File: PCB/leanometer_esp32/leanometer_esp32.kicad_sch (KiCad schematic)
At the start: 5 parts

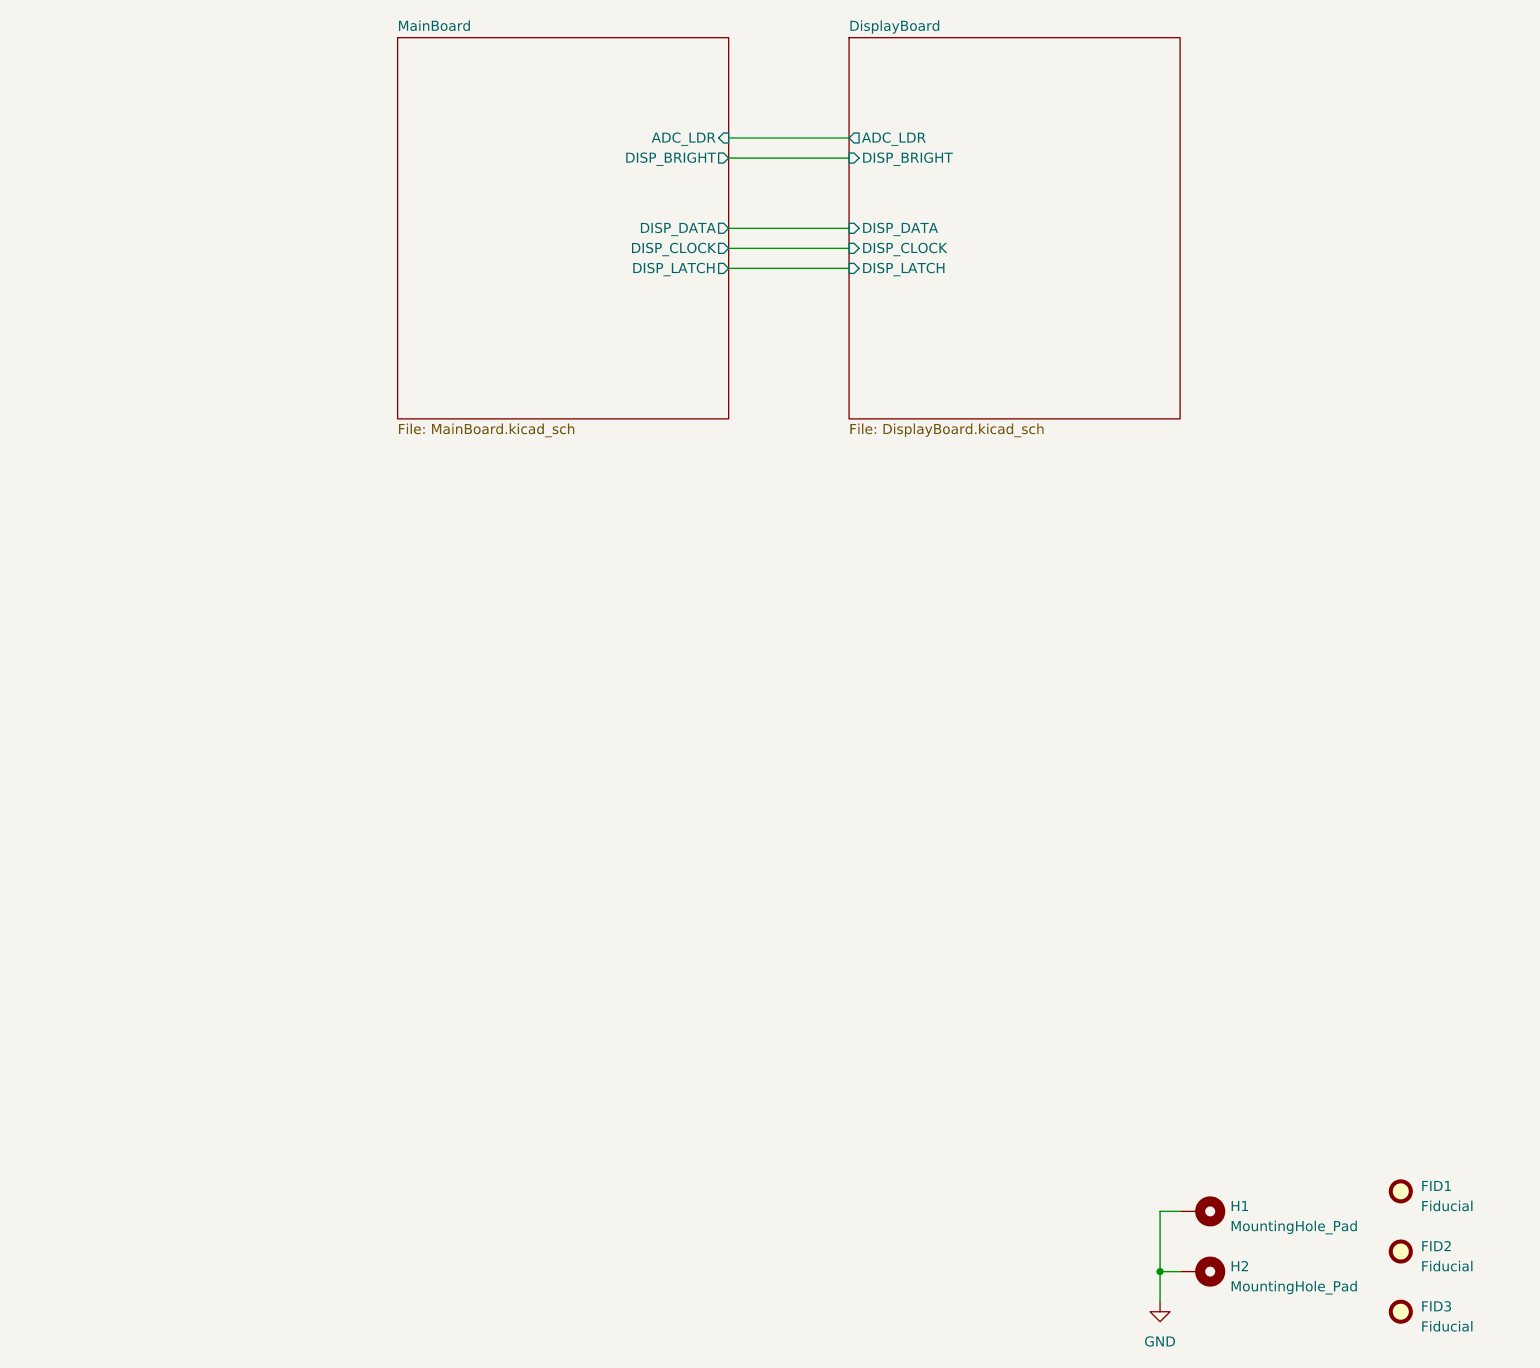
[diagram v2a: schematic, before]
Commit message: Added PowerBoard hierarchical sheet, completed layout
Signed-off-by: theloukou
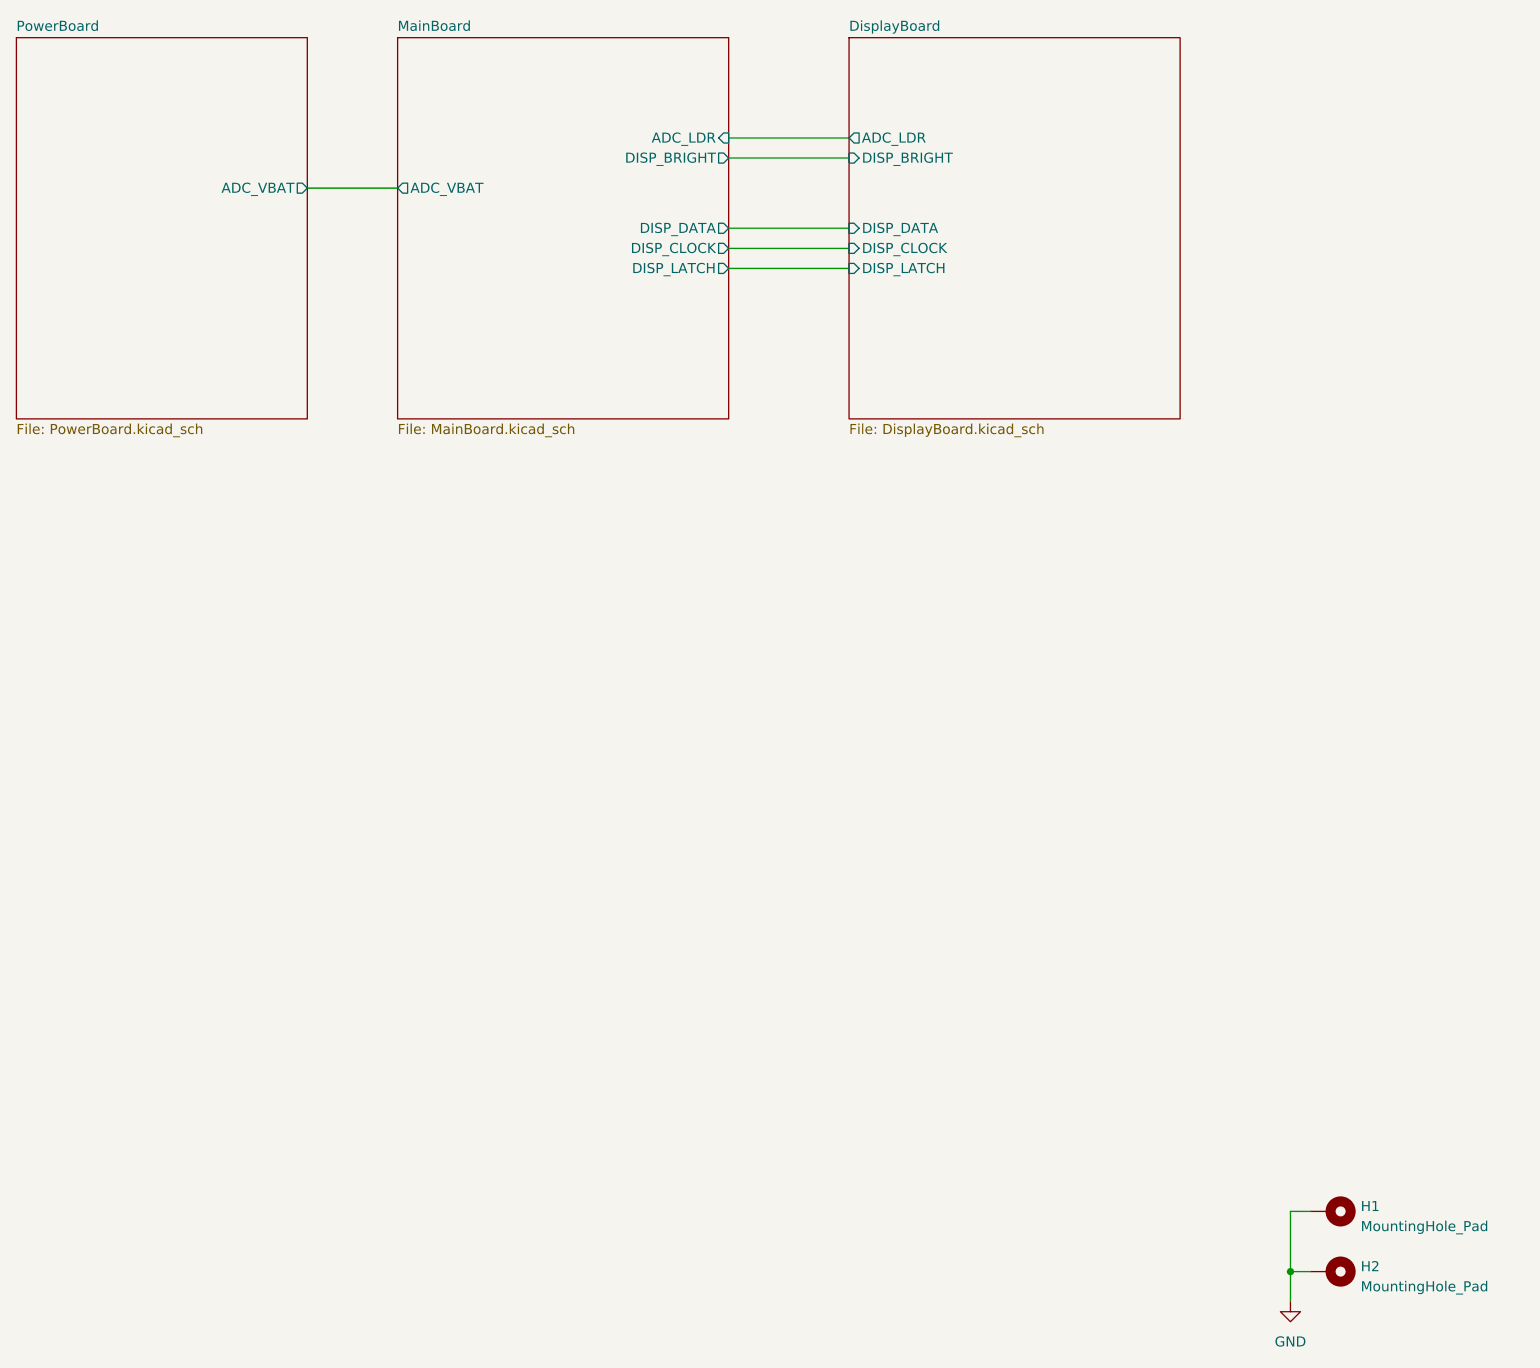
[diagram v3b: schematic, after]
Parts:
- removed FID1, FID2, FID3: Fiducial, Fiducial:Fiducial_0.75mm_Mask1.5mm, symbol Mechanical:Fiducial
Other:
- added sheet PowerBoard (PowerBoard.kicad_sch)
- sheet MainBoard ports: added ADC_VBAT; removed none
- moved on the sheet: H1, H2
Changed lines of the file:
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@@
     (comment 1 "Lefteris Kantakos")
   )
-  (junction (at 254 270.51) (diameter 0) (color 0 0 0 0)
+  (junction (at 270.51 270.51) (diameter 0) (color 0 0 0 0)
   )
   (wire (pts (xy 199.39 143.51) (xy 214.63 143.51))
     (stroke (width 0) (type default))
   )
-  (wire (pts (xy 254 270.51) (xy 256.54 270.51))
+  (wire (pts (xy 270.51 270.51) (xy 273.05 270.51))
     (stroke (width 0) (type default))
   )
@@
     (stroke (width 0) (type default))
   )
-  (wire (pts (xy 254 270.51) (xy 254 274.32))
+  (wire (pts (xy 270.51 270.51) (xy 270.51 274.32))
     (stroke (width 0) (type default))
   )
-  (wire (pts (xy 256.54 262.89) (xy 254 262.89))
+  (wire (pts (xy 146.05 133.35) (xy 157.48 133.35))
+    (stroke (width 0) (type default))
+  )
+  (wire (pts (xy 273.05 262.89) (xy 270.51 262.89))
     (stroke (width 0) (type default))
   )
@@
     (stroke (width 0) (type default))
   )
-  (wire (pts (xy 254 262.89) (xy 254 270.51))
+  (wire (pts (xy 270.51 262.89) (xy 270.51 270.51))
     (stroke (width 0) (type default))
   )
-  (symbol (lib_id "Mechanical:Fiducial") (at 284.48 267.97 0) (unit 1)
+  (symbol (lib_id "power:GND") (at 270.51 274.32 0) (unit 1)
     (in_bom yes) (on_board yes) (dnp no) (fields_autoplaced)
-    (property "Reference" "FID2" (at 287.02 267.335 0)
-      (effects (font (size 1.27 1.27)) (justify left))
-    )
-    (property "Value" "Fiducial" (at 287.02 269.875 0)
-      (effects (font (size 1.27 1.27)) (justify left))
-    )
-    (property "Footprint" "Fiducial:Fiducial_0.75mm_Mask1.5mm" (at 284.48 267.97 0)
+    (property "Reference" "#PWR01" (at 270.51 280.67 0)
       (effects (font (size 1.27 1.27)) hide)
     )
-    (property "Datasheet" "~" (at 284.48 267.97 0)
+    (property "Value" "GND" (at 270.51 279.4 0)
+      (effects (font (size 1.27 1.27)))
+    )
+    (property "Footprint" "" (at 270.51 274.32 0)
       (effects (font (size 1.27 1.27)) hide)
     )
-    (instances
-      (project "leanometer_esp32"
-        (path "/90da9009-635c-418a-81cf-a9914c9a139e"
-          (reference "FID2") (unit 1)
-        )
-      )
-    )
-  )
-  (symbol (lib_id "Mechanical:Fiducial") (at 284.48 275.59 0) (unit 1)
-    (in_bom yes) (on_board yes) (dnp no) (fields_autoplaced)
-    (property "Reference" "FID3" (at 287.02 274.955 0)
-      (effects (font (size 1.27 1.27)) (justify left))
-    )
-    (property "Value" "Fiducial" (at 287.02 277.495 0)
-      (effects (font (size 1.27 1.27)) (justify left))
-    )
-    (property "Footprint" "Fiducial:Fiducial_0.75mm_Mask1.5mm" (at 284.48 275.59 0)
-      (effects (font (size 1.27 1.27)) hide)
-    )
-    (property "Datasheet" "~" (at 284.48 275.59 0)
-      (effects (font (size 1.27 1.27)) hide)
-    )
-    (instances
-      (project "leanometer_esp32"
-        (path "/90da9009-635c-418a-81cf-a9914c9a139e"
-          (reference "FID3") (unit 1)
-        )
-      )
-    )
-  )
-  (symbol (lib_id "power:GND") (at 254 274.32 0) (unit 1)
-    (in_bom yes) (on_board yes) (dnp no) (fields_autoplaced)
-    (property "Reference" "#PWR01" (at 254 280.67 0)
-      (effects (font (size 1.27 1.27)) hide)
-    )
-    (property "Value" "GND" (at 254 279.4 0)
-      (effects (font (size 1.27 1.27)))
-    )
-    (property "Footprint" "" (at 254 274.32 0)
-      (effects (font (size 1.27 1.27)) hide)
-    )
-    (property "Datasheet" "" (at 254 274.32 0)
+    (property "Datasheet" "" (at 270.51 274.32 0)
       (effects (font (size 1.27 1.27)) hide)
     )
@@
     )
   )
-  (symbol (lib_id "Mechanical:MountingHole_Pad") (at 259.08 262.89 270) (unit 1)
+  (symbol (lib_id "Mechanical:MountingHole_Pad") (at 275.59 262.89 270) (unit 1)
     (in_bom yes) (on_board yes) (dnp no) (fields_autoplaced)
-    (property "Reference" "H1" (at 262.89 262.255 90)
+    (property "Reference" "H1" (at 279.4 262.255 90)
       (effects (font (size 1.27 1.27)) (justify left))
     )
-    (property "Value" "MountingHole_Pad" (at 262.89 264.795 90)
+    (property "Value" "MountingHole_Pad" (at 279.4 264.795 90)
       (effects (font (size 1.27 1.27)) (justify left))
     )
-    (property "Footprint" "MountingHole:MountingHole_2.2mm_M2_DIN965_Pad" (at 259.08 262.89 0)
+    (property "Footprint" "MountingHole:MountingHole_2.2mm_M2_DIN965_Pad" (at 275.59 262.89 0)
       (effects (font (size 1.27 1.27)) hide)
     )
-    (property "Datasheet" "~" (at 259.08 262.89 0)
+    (property "Datasheet" "~" (at 275.59 262.89 0)
       (effects (font (size 1.27 1.27)) hide)
     )
@@
     )
   )
-  (symbol (lib_id "Mechanical:MountingHole_Pad") (at 259.08 270.51 270) (unit 1)
+  (symbol (lib_id "Mechanical:MountingHole_Pad") (at 275.59 270.51 270) (unit 1)
     (in_bom yes) (on_board yes) (dnp no) (fields_autoplaced)
-    (property "Reference" "H2" (at 262.89 269.875 90)
+    (property "Reference" "H2" (at 279.4 269.875 90)
       (effects (font (size 1.27 1.27)) (justify left))
     )
-    (property "Value" "MountingHole_Pad" (at 262.89 272.415 90)
+    (property "Value" "MountingHole_Pad" (at 279.4 272.415 90)
       (effects (font (size 1.27 1.27)) (justify left))
     )
-    (property "Footprint" "MountingHole:MountingHole_2.2mm_M2_DIN965_Pad" (at 259.08 270.51 0)
+    (property "Footprint" "MountingHole:MountingHole_2.2mm_M2_DIN965_Pad" (at 275.59 270.51 0)
       (effects (font (size 1.27 1.27)) hide)
     )
-    (property "Datasheet" "~" (at 259.08 270.51 0)
+    (property "Datasheet" "~" (at 275.59 270.51 0)
       (effects (font (size 1.27 1.27)) hide)
     )
@@
         (path "/90da9009-635c-418a-81cf-a9914c9a139e"
           (reference "H2") (unit 1)
-        )
-      )
-    )
-  )
-  (symbol (lib_id "Mechanical:Fiducial") (at 284.48 260.35 0) (unit 1)
-    (in_bom yes) (on_board yes) (dnp no) (fields_autoplaced)
-    (property "Reference" "FID1" (at 287.02 259.715 0)
-      (effects (font (size 1.27 1.27)) (justify left))
-    )
-    (property "Value" "Fiducial" (at 287.02 262.255 0)
-      (effects (font (size 1.27 1.27)) (justify left))
-    )
-    (property "Footprint" "Fiducial:Fiducial_0.75mm_Mask1.5mm" (at 284.48 260.35 0)
-      (effects (font (size 1.27 1.27)) hide)
-    )
-    (property "Datasheet" "~" (at 284.48 260.35 0)
-      (effects (font (size 1.27 1.27)) hide)
-    )
-    (instances
-      (project "leanometer_esp32"
-        (path "/90da9009-635c-418a-81cf-a9914c9a139e"
-          (reference "FID1") (unit 1)
         )
       )
@@
     )
     (pin "DISP_LATCH" output (at 199.39 143.51 0)
+      (effects (font (size 1.27 1.27)) (justify right))
+    )
+    (pin "ADC_VBAT" output (at 157.48 133.35 180)
+      (effects (font (size 1.27 1.27)) (justify left))
+    )
+    (instances
+      (project "leanometer_esp32"
+        (path "/90da9009-635c-418a-81cf-a9914c9a139e" (page "3"))
+      )
+    )
+  )
+  (sheet (at 109.22 114.3) (size 36.83 48.26) (fields_autoplaced)
+    (stroke (width 0.1524) (type solid))
+    (fill (color 0 0 0 0.0000))
+    (property "Sheetname" "PowerBoard" (at 109.22 113.5884 0)
+      (effects (font (size 1.27 1.27)) (justify left bottom))
+    )
+    (property "Sheetfile" "PowerBoard.kicad_sch" (at 109.22 163.1446 0)
+      (effects (font (size 1.27 1.27)) (justify left top))
+    )
+    (pin "ADC_VBAT" output (at 146.05 133.35 0)
       (effects (font (size 1.27 1.27)) (justify right))
     )
@@
     (instances
       (project "leanometer_esp32"
-        (path "/90da9009-635c-418a-81cf-a9914c9a139e" (page "3"))
+        (path "/90da9009-635c-418a-81cf-a9914c9a139e" (page "4"))
       )
     )
